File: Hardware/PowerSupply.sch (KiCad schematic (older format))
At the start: 13 parts, among them U3 LMR50410-Q1

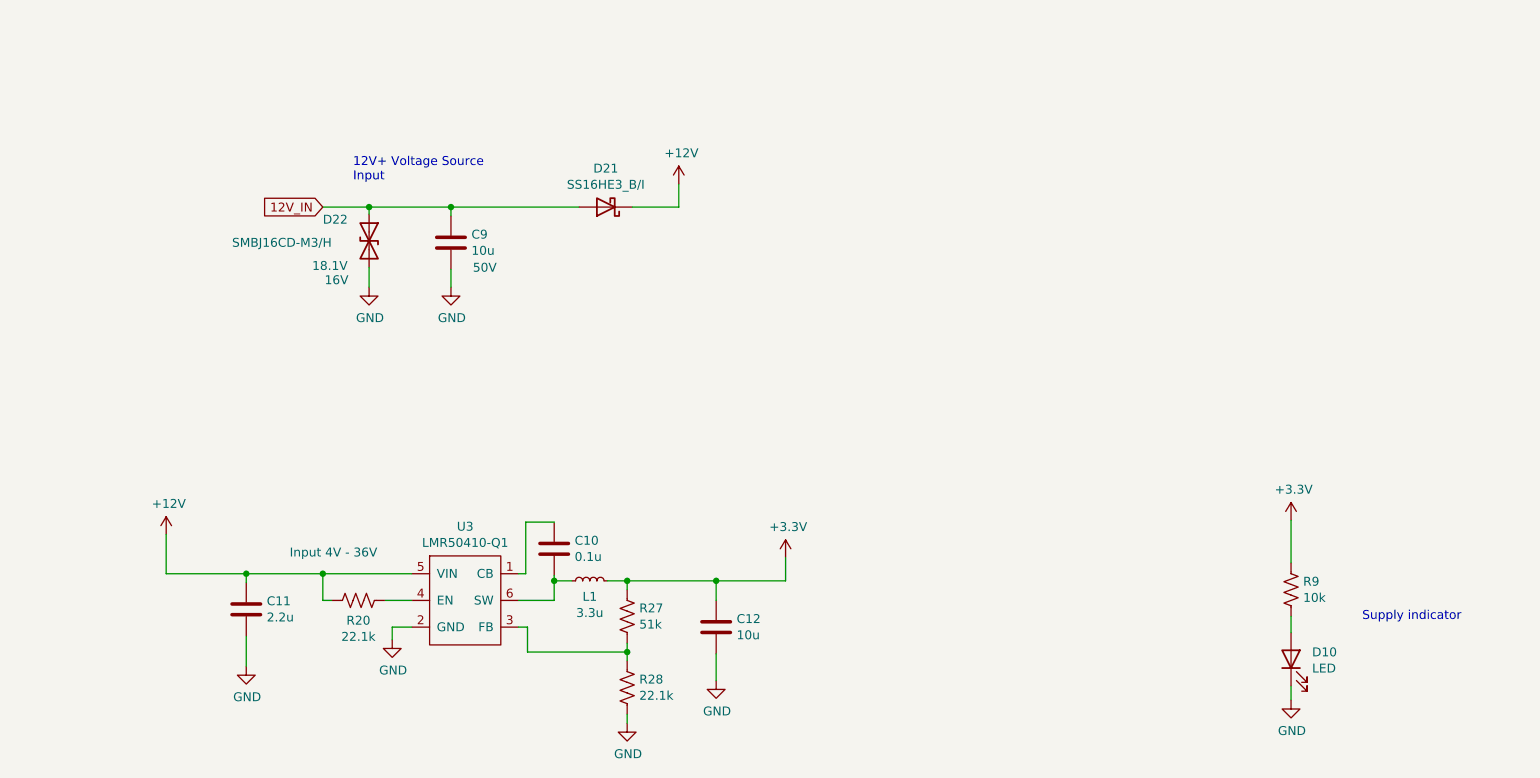
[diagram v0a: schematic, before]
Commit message: Rev B
Update STM package, switcher circuit, layout
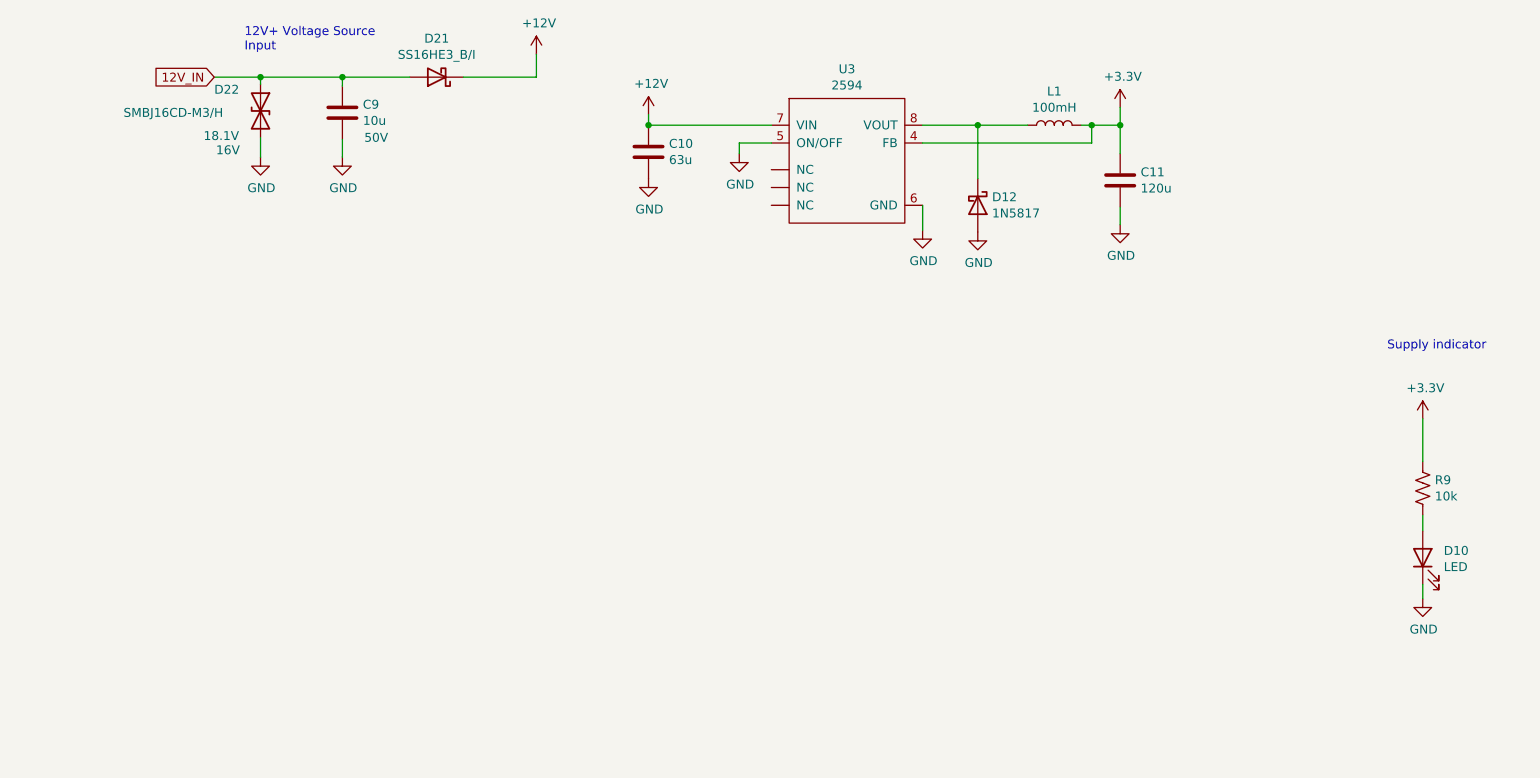
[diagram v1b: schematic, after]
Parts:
- removed C12: 10u, Inductor_SMD:L_0603_1608Metric, symbol Device:C
- removed L1: 3.3u, Inductor_SMD:L_0603_1608Metric_Pad1.05x0.95mm_HandSolder, symbol Device:L_Small
- removed R20, R28: 22.1k, Resistor_SMD:R_0402_1005Metric, symbol Device:R_US
- removed R27: 51k, Resistor_SMD:R_0402_1005Metric, symbol Device:R_US
- removed U3: LMR50410-Q1, Package_TO_SOT_SMD:SOT-23-6, symbol custom:LMR50410-Q1
- added D12: 1N5817, Diode_SMD:D_SOD-123, symbol Diode:1N5817
- added L1: 100mH, Inductor_SMD:L_0603_1608Metric, symbol Device:L
- added U3: 2594, Package_SO:SOIC-8_3.9x4.9mm_P1.27mm, symbol custom:2594
- C10: value 0.1u -> 63u; footprint Capacitor_SMD:C_0402_1005Metric -> Inductor_SMD:L_0603_1608Metric
- C11: value 2.2u -> 120u; footprint Inductor_SMD:L_1206_3216Metric -> Inductor_SMD:L_0603_1608Metric
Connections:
- net +12V: now also C10.1, U3.7 (VIN); no longer C11.1
- net +3V3: now also C11.1, L1.2, U3.4 (FB)
- net GND: now also C10.2, D12.2 (A), U3.5 (ON/OFF), U3.6 (GND)
- new net: D12.1 (K), L1.1, U3.8 (VOUT)
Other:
- moved on the sheet: C9, D10, D21, D22, R9

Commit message: Update components for assembly, generate gerbers
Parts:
- C10: value 63u -> 10u; Comment (none) -> X5R ±10% 50V 10uF 1206 Multilayer Ceramic Capacitors MLCC -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; LCSC (none) -> C13585; Voltage (none) -> 50v
- C11: footprint Inductor_SMD:L_0603_1608Metric -> Capacitor_SMD:C_1206_3216Metric; Comments (none) -> X5R 100uF 6.3V ±20% 1206 Multilayer Ceramic Capacitors MLCC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; LCSC (none) -> C15008
- C9: Comment (none) -> X5R ±10% 50V 10uF 1206 Multilayer Ceramic Capacitors MLCC -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; LCSC (none) -> C13585
- D10: Comments (none) -> Red 615~630nm 1.9~2.2V 0603 Light Emitting Diodes (LED) RoHS; LCSC (none) -> C2286
- D21: Comment (none) -> 60V 1A 700mV @ 1A SMA Schottky Barrier Diodes (SBD) ROHS; LCSC (none) -> C211772
- D22: Comment (none) -> Bidirectional 23.1A 26V 17.8V 16V SMB(DO-214AA) TVS; LCSC (none) -> C8830
- L1: value 100mH -> 100uH; footprint Inductor_SMD:L_0603_1608Metric -> Inductor_SMD:L_0805_2012Metric; Comments (none) -> 0805 Inductors (SMD) ROHS 100uH; LCSC (none) -> C68035
- R9: value 10k -> 1k; Comments (none) -> ±1% 1/16W ±100ppm/℃ 1kΩ 0402 Chip Resistor - Surface Mount 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; LCSC (none) -> C11702
- U3: Comments (none) -> 500mA 40V SOP-8 DC-DC Converters ROHS; LCSC (none) -> C316691
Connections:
- no-connect marks 0 -> 3

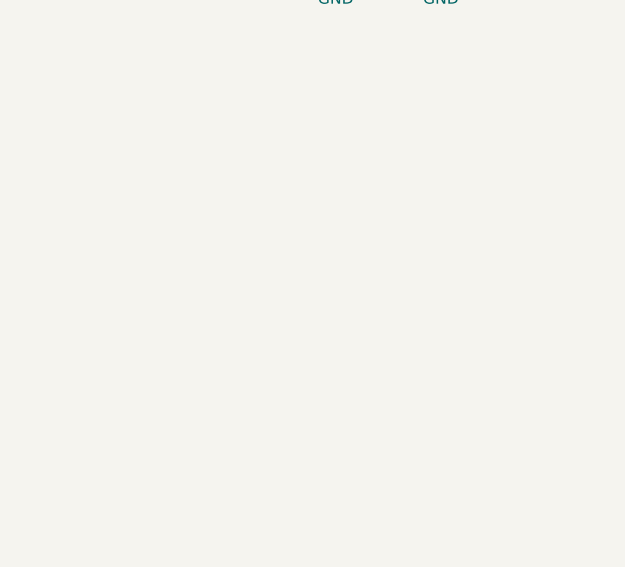
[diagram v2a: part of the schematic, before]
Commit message: Update board layout
Fix OLED pads to meet intended design. Move all non UI components to one side of the board for better single sided assembly.
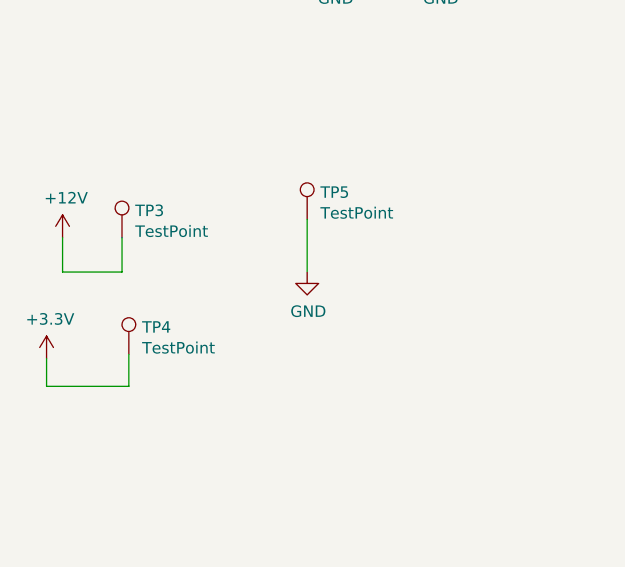
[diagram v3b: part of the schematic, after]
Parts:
- added TP3, TP4, TP5: TestPoint, TestPoint:TestPoint_Pad_D1.0mm, symbol Connector:TestPoint
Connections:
- net +12V: now also TP3.1
- net +3V3: now also TP4.1
- net GND: now also TP5.1
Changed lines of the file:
@@
 	1    0    0    -1
 $EndComp
+$Comp
+L Connector:TestPoint TP?
+U 1 1 61B7485F
+P 2000 3540
+AR Path="/615E5281/61B7485F" Ref="TP?"  Part="1"
+AR Path="/615E7CAC/61B7485F" Ref="TP3"  Part="1"
+F 0 "TP3" H 2058 3658 50  0000 L CNN
+F 1 "TestPoint" H 2058 3567 50  0000 L CNN
+F 2 "TestPoint:TestPoint_Pad_D1.0mm" H 2200 3540 50  0001 C CNN
+F 3 "~" H 2200 3540 50  0001 C CNN
+	1    2000 3540
+	1    0    0    -1
+$EndComp
+$Comp
+L Connector:TestPoint TP?
+U 1 1 61B74D64
+P 2030 4050
+AR Path="/615E5281/61B74D64" Ref="TP?"  Part="1"
+AR Path="/615E7CAC/61B74D64" Ref="TP4"  Part="1"
+F 0 "TP4" H 2088 4168 50  0000 L CNN
+F 1 "TestPoint" H 2088 4077 50  0000 L CNN
+F 2 "TestPoint:TestPoint_Pad_D1.0mm" H 2088 4031 50  0001 L CNN
+F 3 "~" H 2230 4050 50  0001 C CNN
+	1    2030 4050
+	1    0    0    -1
+$EndComp
+$Comp
+L Connector:TestPoint TP?
+U 1 1 61B7528A
+P 2810 3460
+AR Path="/615E5281/61B7528A" Ref="TP?"  Part="1"
+AR Path="/615E7CAC/61B7528A" Ref="TP5"  Part="1"
+F 0 "TP5" H 2868 3578 50  0000 L CNN
+F 1 "TestPoint" H 2868 3487 50  0000 L CNN
+F 2 "TestPoint:TestPoint_Pad_D1.0mm" H 3010 3460 50  0001 C CNN
+F 3 "~" H 3010 3460 50  0001 C CNN
+	1    2810 3460
+	1    0    0    -1
+$EndComp
+$Comp
+L power:+12V #PWR0165
+U 1 1 61B75EAD
+P 1740 3540
+F 0 "#PWR0165" H 1740 3390 50  0001 C CNN
+F 1 "+12V" H 1755 3713 50  0000 C CNN
+F 2 "" H 1740 3540 50  0001 C CNN
+F 3 "" H 1740 3540 50  0001 C CNN
+	1    1740 3540
+	1    0    0    -1
+$EndComp
+$Comp
+L power:+3.3V #PWR0166
+U 1 1 61B773FF
+P 1670 4070
+F 0 "#PWR0166" H 1670 3920 50  0001 C CNN
+F 1 "+3.3V" H 1685 4243 50  0000 C CNN
+F 2 "" H 1670 4070 50  0001 C CNN
+F 3 "" H 1670 4070 50  0001 C CNN
+	1    1670 4070
+	1    0    0    -1
+$EndComp
+$Comp
+L power:GND #PWR0167
+U 1 1 61B77EDD
+P 2810 3690
+F 0 "#PWR0167" H 2810 3440 50  0001 C CNN
+F 1 "GND" H 2815 3517 50  0000 C CNN
+F 2 "" H 2810 3690 50  0001 C CNN
+F 3 "" H 2810 3690 50  0001 C CNN
+	1    2810 3690
+	1    0    0    -1
+$EndComp
+Wire Wire Line
+	2810 3460 2810 3690
+Wire Wire Line
+	2030 4050 2030 4190
+Wire Wire Line
+	2030 4190 1670 4190
+Wire Wire Line
+	1670 4190 1670 4070
+Wire Wire Line
+	2000 3540 2000 3690
+Wire Wire Line
+	2000 3690 1740 3690
+Wire Wire Line
+	1740 3690 1740 3540
 $EndSCHEMATC

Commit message: Updates
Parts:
- added TP7, TP8: TestPoint, TestPoint:TestPoint_Pad_D1.0mm, symbol Connector:TestPoint
- C10: footprint Inductor_SMD:L_0603_1608Metric -> Inductor_SMD:L_1206_3216Metric; LCSC C13585 -> (none)
- L1: LCSC C68035 -> C68035
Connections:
- net +3V3: now also TP7.1
- net GND: now also TP8.1
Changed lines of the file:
@@
 Title "CAN Gauge"
 Date "2021-10-10"
-Rev "B"
+Rev "C"
 Comp ""
 Comment1 ""
@@
 F 0 "C10" H 5225 2336 50  0000 L CNN
 F 1 "10u" H 5225 2245 50  0000 L CNN
-F 2 "Inductor_SMD:L_0603_1608Metric" H 5148 2140 50  0001 C CNN
+F 2 "Inductor_SMD:L_1206_3216Metric" H 5148 2140 50  0001 C CNN
 F 3 "" H 5110 2290 50  0001 C CNN
 F 4 "50v" H 5300 2150 50  0000 C CNN "Voltage"
 F 5 "" H 5110 2290 50  0001 C CNN "Part Number"
 F 6 "" H 5110 2290 50  0001 C CNN "Manufactuer"
-F 7 " C13585" H 5110 2290 50  0001 C CNN "LCSC"
+F 7 "" H 5110 2290 50  0001 C CNN "LCSC"
 F 8 "X5R ±10% 50V 10uF 1206 Multilayer Ceramic Capacitors MLCC - SMD/SMT ROHS" H 5110 2290 50  0001 C CNN "Comment"
 	1    5110 2290
@@
 F 2 "Inductor_SMD:L_0805_2012Metric" H 7390 2140 50  0001 C CNN
 F 3 "~" H 7390 2140 50  0001 C CNN
-F 4 " C68035 " V 7390 2140 50  0001 C CNN "LCSC"
+F 4 "C68035 " V 7390 2140 50  0001 C CNN "LCSC"
 F 5 "0805 Inductors (SMD) ROHS 100uH" V 7390 2140 50  0001 C CNN "Comments"
 	1    7390 2140
@@
 $EndComp
 Wire Wire Line
-	2810 3460 2810 3690
+	2810 3460 2810 3580
 Wire Wire Line
 	2030 4050 2030 4190
@@
 Wire Wire Line
 	1740 3690 1740 3540
+$Comp
+L Connector:TestPoint TP?
+U 1 1 61B79F3B
+P 2530 4060
+AR Path="/615E5281/61B79F3B" Ref="TP?"  Part="1"
+AR Path="/615E7CAC/61B79F3B" Ref="TP7"  Part="1"
+F 0 "TP7" H 2588 4178 50  0000 L CNN
+F 1 "TestPoint" H 2588 4087 50  0000 L CNN
+F 2 "TestPoint:TestPoint_Pad_D1.0mm" H 2588 4041 50  0001 L CNN
+F 3 "~" H 2730 4060 50  0001 C CNN
+	1    2530 4060
+	1    0    0    -1
+$EndComp
+Wire Wire Line
+	2530 4060 2530 4190
+Wire Wire Line
+	2530 4190 2030 4190
+Connection ~ 2030 4190
+$Comp
+L Connector:TestPoint TP?
+U 1 1 61B7B6C1
+P 3350 3460
+AR Path="/615E5281/61B7B6C1" Ref="TP?"  Part="1"
+AR Path="/615E7CAC/61B7B6C1" Ref="TP8"  Part="1"
+F 0 "TP8" H 3408 3578 50  0000 L CNN
+F 1 "TestPoint" H 3408 3487 50  0000 L CNN
+F 2 "TestPoint:TestPoint_Pad_D1.0mm" H 3550 3460 50  0001 C CNN
+F 3 "~" H 3550 3460 50  0001 C CNN
+	1    3350 3460
+	1    0    0    -1
+$EndComp
+Wire Wire Line
+	3350 3460 3350 3580
+Wire Wire Line
+	3350 3580 2810 3580
+Connection ~ 2810 3580
+Wire Wire Line
+	2810 3580 2810 3690
 $EndSCHEMATC
